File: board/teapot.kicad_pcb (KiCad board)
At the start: 2 copper layers, 50 x 50 mm, 41 parts, among them P1 BATT, P2 SMA, Q1 TEPT4400, U1 TPS79333DBVR, U2 TLV61225, U3 microusb-b, U4 RFM69W, U5 STM32L052K8, U6 HTU21D, U7 MS5637, U8 SWD, Y1 32.768k

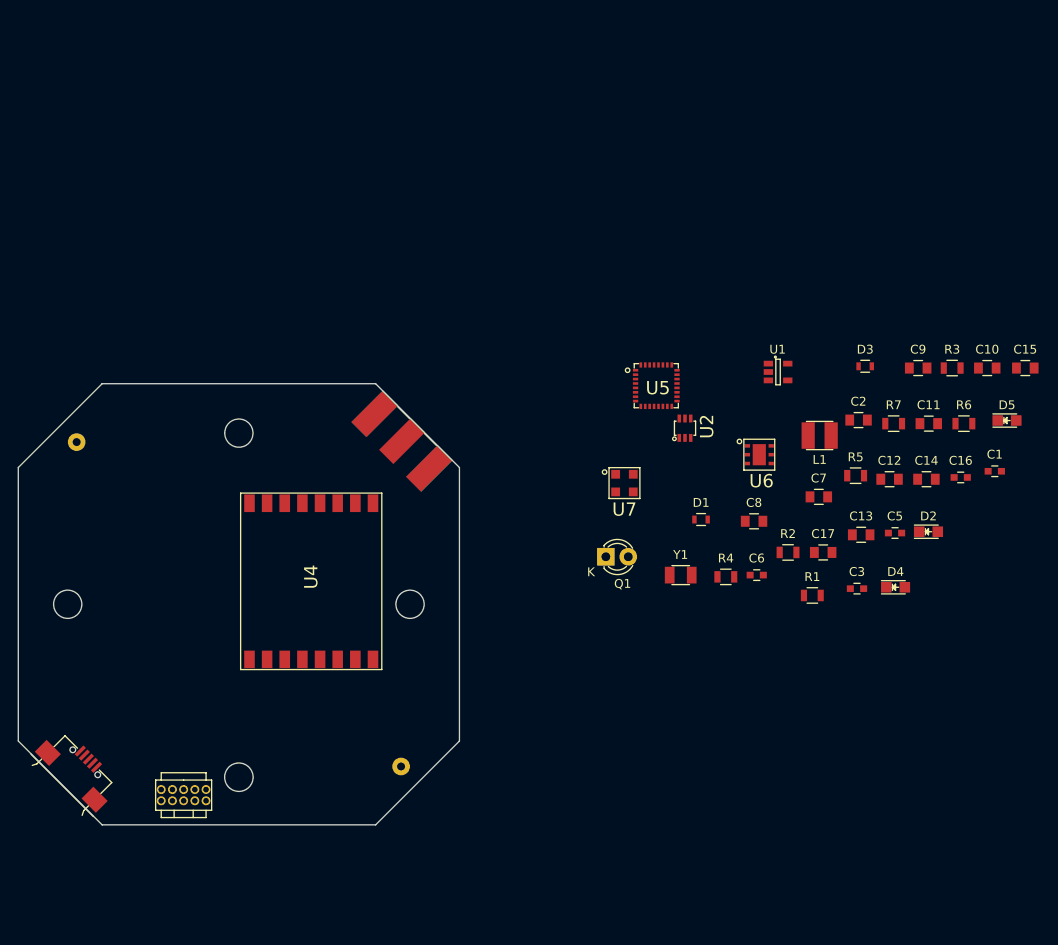
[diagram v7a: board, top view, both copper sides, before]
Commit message: Initial placement and first successful route.
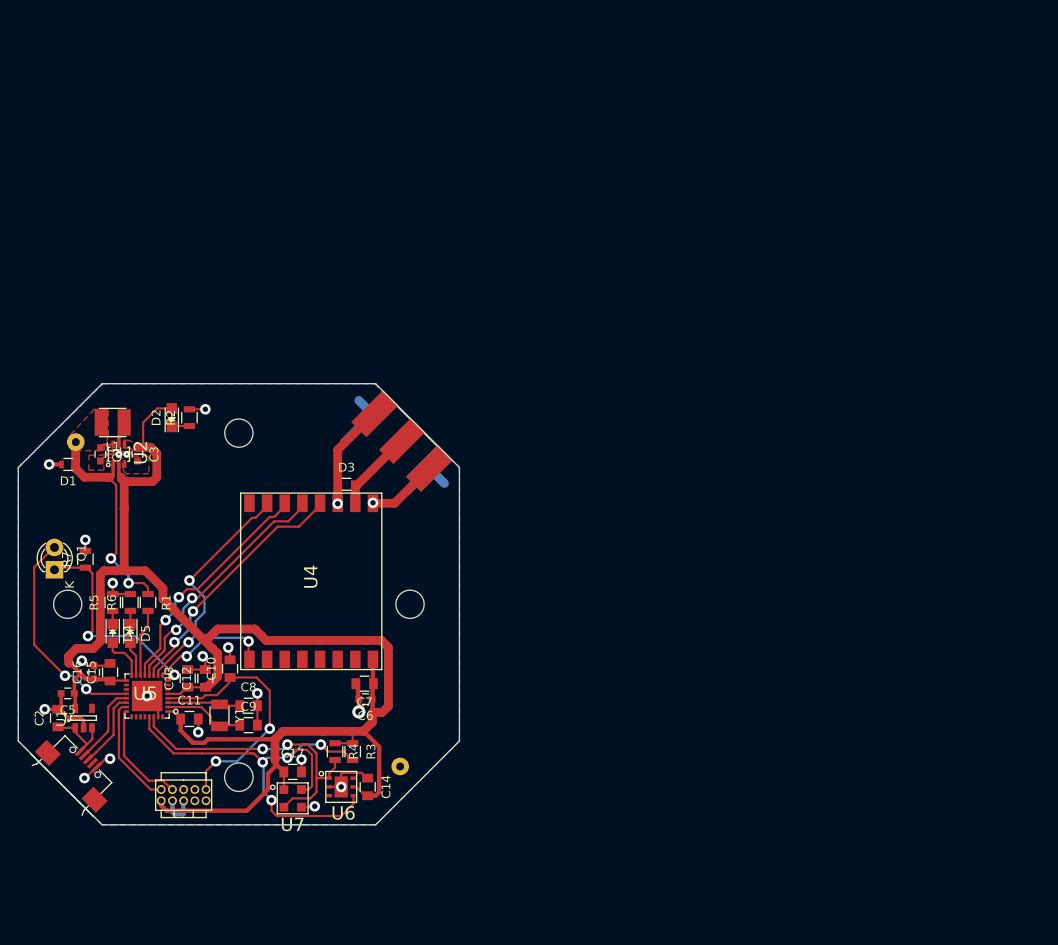
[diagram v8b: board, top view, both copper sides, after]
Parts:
- P1: moved to F.Cu
- moved C15 109.3 mm to (112.4, 120.7), turned to 90 degrees
- moved D5 102.2 mm to (114.7, 116.3), turned to 270 degrees
- moved C1 101.4 mm to (111.3, 96.0), turned to 270 degrees
- moved C16 100.7 mm to (110.6, 120.7), turned to 90 degrees
- moved C2 96.8 mm to (106.5, 125.9), turned to 90 degrees
- moved R6 96.6 mm to (114.7, 112.8), turned to 90 degrees
- moved C5 95.5 mm to (107.6, 123.1), turned to 180 degrees
- moved R7 92.9 mm to (109.6, 107.9), turned to 90 degrees
- moved C10 92.3 mm to (126.0, 120.3), turned to 90 degrees
- moved C11 90.2 mm to (121.4, 126.0)
- moved D4 88.9 mm to (112.7, 116.3), turned to 270 degrees
- moved U1 87.9 mm to (109.4, 125.9), turned to 90 degrees
- moved D2 86.7 mm to (119.4, 91.8), turned to 90 degrees
- moved C9 86.0 mm to (128.1, 126.7)
- moved R5 85.4 mm to (112.7, 112.8), turned to 90 degrees
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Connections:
- C12 pad 1: Net-(C12-Pad1) -> +3V3
- C13 pad 1: Net-(C12-Pad1) -> +3V3
- C3 pad 1: Net-(C3-Pad1) -> +3V3
- D4 pad 2: (no net) -> /LED_GREEN
- D5 pad 2: (no net) -> /LED_YELLOW
- Q1 pad 2: (no net) -> /LIGHT_EN
- R1 pad 2: (no net) -> /BATT_MON
- U2 pad 2: Net-(C3-Pad1) -> +3V3
- U4 pad 1: (no net) -> /RFM_RESET
- U4 pad 12: (no net) -> /RFM_SCK
- U4 pad 13: (no net) -> /RFM_MISO
- U4 pad 14: (no net) -> /RFM_MOSI
- U4 pad 15: (no net) -> /RFM_NSS
- U5 pad 10: (no net) -> /RFM_NSS
- U5 pad 11: (no net) -> /RFM_SCK
- U5 pad 12: (no net) -> /RFM_MISO
- U5 pad 13: (no net) -> /RFM_MOSI
- U5 pad 14: (no net) -> /BATT_MON
- U5 pad 15: (no net) -> /LED_YELLOW
- U5 pad 16: (no net) -> /LED_GREEN
- U5 pad 20: (no net) -> /LIGHT_EN
- U5 pad 5: Net-(C12-Pad1) -> +3V3
- U5 pad 8: (no net) -> /LIGHT_SENSE
- U5 pad 9: (no net) -> /RFM_RESET
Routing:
- net +3V3: track 0.00 -> 184.6 mm
- net GND: track 0.00 -> 93.0 mm, vias 0 -> 21
- net /I2C_SCK: track 0.00 -> 53.0 mm, vias 0 -> 4
- net /I2C_SDA: track 0.00 -> 33.9 mm, vias 0 -> 2
- net /RFM_SCK: track 0.00 -> 29.8 mm, vias 0 -> 2
- net /nRST: track 0.00 -> 29.1 mm, vias 0 -> 2
- net /RFM_MISO: track 0.00 -> 28.9 mm, vias 0 -> 2
- net /RFM_MOSI: track 0.00 -> 27.8 mm, vias 0 -> 2
- net Net-(C1-Pad1): track 0.00 -> 27.4 mm, vias 0 -> 2
- net /RFM_NSS: track 0.00 -> 27.1 mm, vias 0 -> 2
- net /LIGHT_SENSE: track 0.00 -> 25.0 mm, vias 0 -> 2
- net /LIGHT_EN: track 0.00 -> 24.8 mm, vias 0 -> 2
- net /RFM_RESET: track 0.00 -> 14.1 mm, vias 0 -> 2
- net /SWDIO: track 0.00 -> 12.7 mm
- net /SWCLK: track 0.00 -> 12.2 mm
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- added copper zone on F.Cu, net +3V3
- added copper zone on B.Cu, net GND
- added copper zone on F.Cu, net GND
- added copper zone on F.Cu, net Net-(C1-Pad1)
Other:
- net class Default: clearance 0.2 -> 0.1; via_dia 0.6 -> 1.2; via_drill 0.4 -> 0.6
- rule trace_clearance: 0.2 -> 0.1
- rule trace_min: 0.2 -> 0.25
- rule via_min_drill: 0.3 -> 0.2
- rule via_min_size: 0.4 -> 0.8
